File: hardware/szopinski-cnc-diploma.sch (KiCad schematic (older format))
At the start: 26 parts, among them J1 Barrel_Jack, J2 Conn_02x08_Odd_Even, J3 AVR-ISP-10, J4 Conn_01x04, J5 Conn_01x04, J6 Conn_01x04, J7 Conn_01x04, U1 ATmega328P-PU, U2 L7805, U3 DRV8825, U4 DRV8825, U5 DRV8825, U6 DRV8825, Y1 20 MHz

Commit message: Add PCB without traces
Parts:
- C1: footprint (none) -> Capacitor_THT:CP_Radial_D4.0mm_P1.50mm
- C2, C3, C4, C9: footprint (none) -> Capacitor_SMD:C_0201_0603Metric
- C5, C6, C7, C8: footprint (none) -> Capacitor_THT:CP_Radial_D6.3mm_P2.50mm
- J1: footprint (none) -> Connector_BarrelJack:BarrelJack_Horizontal
- J2: footprint (none) -> Connector_PinHeader_2.54mm:PinHeader_2x08_P2.54mm_Vertical
- J3: footprint (none) -> Connector_PinHeader_2.54mm:PinHeader_2x05_P2.54mm_Vertical
- J4, J5, J6, J7: footprint (none) -> Connector_Molex:Molex_KK-254_AE-6410-04A_1x04_P2.54mm_Vertical
- R1, R2, R3: footprint (none) -> Resistor_SMD:R_0201_0603Metric
- U2: footprint (none) -> Package_TO_SOT_THT:TO-220-3_Horizontal_TabDown
- U3, U4, U5, U6: footprint (none) -> Package_DIP:DIP-16_W15.24mm
- Y1: footprint (none) -> Crystal:Crystal_HC49-4H_Vertical
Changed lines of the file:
@@
 F 0 "U2" H 3200 1392 50  0000 C CNN
 F 1 "L7805" H 3200 1301 50  0000 C CNN
-F 2 "" H 3225 1000 50  0001 L CIN
+F 2 "Package_TO_SOT_THT:TO-220-3_Horizontal_TabDown" H 3225 1000 50  0001 L CIN
 F 3 "http://www.st.com/content/ccc/resource/technical/document/datasheet/41/4f/b3/b0/12/d4/47/88/CD00000444.pdf/files/CD00000444.pdf/jcr:content/translations/en.CD00000444.pdf" H 3200 1100 50  0001 C CNN
 	1    3200 1150
@@
 F 0 "J1" H 1407 1575 50  0000 C CNN
 F 1 "Barrel_Jack" H 1407 1484 50  0000 C CNN
-F 2 "" H 1400 1210 50  0001 C CNN
+F 2 "Connector_BarrelJack:BarrelJack_Horizontal" H 1400 1210 50  0001 C CNN
 F 3 "~" H 1400 1210 50  0001 C CNN
 	1    1350 1250
@@
 F 0 "C1" H 2618 1546 50  0000 L CNN
 F 1 "470n" H 2618 1455 50  0000 L CNN
-F 2 "" H 2538 1350 50  0001 C CNN
+F 2 "Capacitor_THT:CP_Radial_D4.0mm_P1.50mm" H 2538 1350 50  0001 C CNN
 F 3 "~" H 2500 1500 50  0001 C CNN
 	1    2500 1500
@@
 F 0 "C2" H 4315 1546 50  0000 L CNN
 F 1 "100n" H 4315 1455 50  0000 L CNN
-F 2 "" H 4238 1350 50  0001 C CNN
+F 2 "Capacitor_SMD:C_0201_0603Metric" H 4238 1350 50  0001 C CNN
 F 3 "~" H 4200 1500 50  0001 C CNN
 	1    4200 1500
@@
 F 0 "C3" H 4365 4596 50  0000 L CNN
 F 1 "22p" H 4365 4505 50  0000 L CNN
-F 2 "" H 4288 4400 50  0001 C CNN
+F 2 "Capacitor_SMD:C_0201_0603Metric" H 4288 4400 50  0001 C CNN
 F 3 "~" H 4250 4550 50  0001 C CNN
 	1    4250 4550
@@
 F 0 "Y1" H 4500 4518 50  0000 C CNN
 F 1 "20 MHz" H 4500 4427 50  0000 C CNN
-F 2 "" H 4500 4250 50  0001 C CNN
+F 2 "Crystal:Crystal_HC49-4H_Vertical" H 4500 4250 50  0001 C CNN
 F 3 "~" H 4500 4250 50  0001 C CNN
 	1    4500 4250
@@
 F 0 "R1" H 3620 4596 50  0000 L CNN
 F 1 "10k" H 3620 4505 50  0000 L CNN
-F 2 "" V 3480 4550 50  0001 C CNN
+F 2 "Resistor_SMD:R_0201_0603Metric" V 3480 4550 50  0001 C CNN
 F 3 "~" H 3550 4550 50  0001 C CNN
 	1    3550 4550
@@
 F 0 "J3" H 4470 3396 50  0000 R CNN
 F 1 "AVR-ISP-10" H 4470 3305 50  0000 R CNN
-F 2 "" V 4550 3350 50  0001 C CNN
+F 2 "Connector_PinHeader_2.54mm:PinHeader_2x05_P2.54mm_Vertical" V 4550 3350 50  0001 C CNN
 F 3 " ~" H 3525 2750 50  0001 C CNN
 	1    4800 3300
@@
 F 0 "C4" H 4865 4596 50  0000 L CNN
 F 1 "22p" H 4865 4505 50  0000 L CNN
-F 2 "" H 4788 4400 50  0001 C CNN
+F 2 "Capacitor_SMD:C_0201_0603Metric" H 4788 4400 50  0001 C CNN
 F 3 "~" H 4750 4550 50  0001 C CNN
 	1    4750 4550
@@
 F 0 "C5" V 6145 1500 50  0000 C CNN
 F 1 "CP" V 6236 1500 50  0000 C CNN
-F 2 "" H 6438 1350 50  0001 C CNN
+F 2 "Capacitor_THT:CP_Radial_D6.3mm_P2.50mm" H 6438 1350 50  0001 C CNN
 F 3 "~" H 6400 1500 50  0001 C CNN
 	1    6400 1500
@@
 F 0 "J4" V 7164 1112 50  0000 R CNN
 F 1 "Conn_01x04" V 7073 1112 50  0000 R CNN
-F 2 "" H 7200 1400 50  0001 C CNN
+F 2 "Connector_Molex:Molex_KK-254_AE-6410-04A_1x04_P2.54mm_Vertical" H 7200 1400 50  0001 C CNN
 F 3 "~" H 7200 1400 50  0001 C CNN
 	1    7200 1400
@@
 F 0 "C7" V 9045 1500 50  0000 C CNN
 F 1 "CP" V 9136 1500 50  0000 C CNN
-F 2 "" H 9338 1350 50  0001 C CNN
+F 2 "Capacitor_THT:CP_Radial_D6.3mm_P2.50mm" H 9338 1350 50  0001 C CNN
 F 3 "~" H 9300 1500 50  0001 C CNN
 	1    9300 1500
@@
 F 0 "J6" V 10064 1112 50  0000 R CNN
 F 1 "Conn_01x04" V 9973 1112 50  0000 R CNN
-F 2 "" H 10100 1400 50  0001 C CNN
+F 2 "Connector_Molex:Molex_KK-254_AE-6410-04A_1x04_P2.54mm_Vertical" H 10100 1400 50  0001 C CNN
 F 3 "~" H 10100 1400 50  0001 C CNN
 	1    10100 1400
@@
 F 0 "C6" V 6145 4100 50  0000 C CNN
 F 1 "CP" V 6236 4100 50  0000 C CNN
-F 2 "" H 6438 3950 50  0001 C CNN
+F 2 "Capacitor_THT:CP_Radial_D6.3mm_P2.50mm" H 6438 3950 50  0001 C CNN
 F 3 "~" H 6400 4100 50  0001 C CNN
 	1    6400 4100
@@
 F 0 "J5" V 7164 3712 50  0000 R CNN
 F 1 "Conn_01x04" V 7073 3712 50  0000 R CNN
-F 2 "" H 7200 4000 50  0001 C CNN
+F 2 "Connector_Molex:Molex_KK-254_AE-6410-04A_1x04_P2.54mm_Vertical" H 7200 4000 50  0001 C CNN
 F 3 "~" H 7200 4000 50  0001 C CNN
 	1    7200 4000
@@
 F 0 "C8" V 9045 4100 50  0000 C CNN
 F 1 "CP" V 9136 4100 50  0000 C CNN
-F 2 "" H 9338 3950 50  0001 C CNN
+F 2 "Capacitor_THT:CP_Radial_D6.3mm_P2.50mm" H 9338 3950 50  0001 C CNN
 F 3 "~" H 9300 4100 50  0001 C CNN
 	1    9300 4100
@@
 F 0 "J7" V 10064 3712 50  0000 R CNN
 F 1 "Conn_01x04" V 9973 3712 50  0000 R CNN
-F 2 "" H 10100 4000 50  0001 C CNN
+F 2 "Connector_Molex:Molex_KK-254_AE-6410-04A_1x04_P2.54mm_Vertical" H 10100 4000 50  0001 C CNN
 F 3 "~" H 10100 4000 50  0001 C CNN
 	1    10100 4000
@@
 F 0 "U3" H 7528 1096 50  0000 L CNN
 F 1 "DRV8825" H 7528 1005 50  0000 L CNN
-F 2 "" H 7550 1100 50  0001 C CNN
+F 2 "Package_DIP:DIP-16_W15.24mm" H 7550 1100 50  0001 C CNN
 F 3 "" H 7550 1100 50  0001 C CNN
 	1    6850 1700
@@
 F 0 "U5" H 10428 1096 50  0000 L CNN
 F 1 "DRV8825" H 10428 1005 50  0000 L CNN
-F 2 "" H 10450 1100 50  0001 C CNN
+F 2 "Package_DIP:DIP-16_W15.24mm" H 10450 1100 50  0001 C CNN
 F 3 "" H 10450 1100 50  0001 C CNN
 	1    9750 1700
@@
 F 0 "U6" H 10428 3696 50  0000 L CNN
 F 1 "DRV8825" H 10428 3605 50  0000 L CNN
-F 2 "" H 10450 3700 50  0001 C CNN
+F 2 "Package_DIP:DIP-16_W15.24mm" H 10450 3700 50  0001 C CNN
 F 3 "" H 10450 3700 50  0001 C CNN
 	1    9750 4300
@@
 F 0 "U4" H 7528 3696 50  0000 L CNN
 F 1 "DRV8825" H 7528 3605 50  0000 L CNN
-F 2 "" H 7550 3700 50  0001 C CNN
+F 2 "Package_DIP:DIP-16_W15.24mm" H 7550 3700 50  0001 C CNN
 F 3 "" H 7550 3700 50  0001 C CNN
 	1    6850 4300
@@
 F 0 "R2" H 5520 5196 50  0000 L CNN
 F 1 "10k" H 5520 5105 50  0000 L CNN
-F 2 "" V 5380 5150 50  0001 C CNN
+F 2 "Resistor_SMD:R_0201_0603Metric" V 5380 5150 50  0001 C CNN
 F 3 "~" H 5450 5150 50  0001 C CNN
 	1    5450 5150
@@
 F 0 "R3" H 5570 2146 50  0000 L CNN
 F 1 "10k" H 5570 2055 50  0000 L CNN
-F 2 "" V 5430 2100 50  0001 C CNN
+F 2 "Resistor_SMD:R_0201_0603Metric" V 5430 2100 50  0001 C CNN
 F 3 "~" H 5500 2100 50  0001 C CNN
 	1    5500 2100
@@
 F 0 "J2" H 4500 6917 50  0000 C CNN
 F 1 "Conn_02x08_Odd_Even" H 4500 6826 50  0000 C CNN
-F 2 "" H 4450 6400 50  0001 C CNN
+F 2 "Connector_PinHeader_2.54mm:PinHeader_2x08_P2.54mm_Vertical" H 4450 6400 50  0001 C CNN
 F 3 "~" H 4450 6400 50  0001 C CNN
 	1    4450 6400
@@
 F 0 "C9" V 1748 2600 50  0000 C CNN
 F 1 "100n" V 1839 2600 50  0000 C CNN
-F 2 "" H 2038 2450 50  0001 C CNN
+F 2 "Capacitor_SMD:C_0201_0603Metric" H 2038 2450 50  0001 C CNN
 F 3 "~" H 2000 2600 50  0001 C CNN
 	1    2000 2600

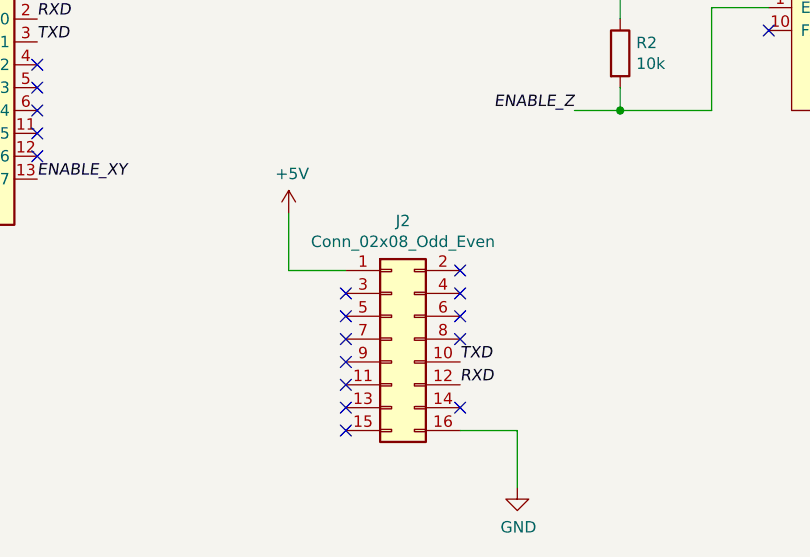
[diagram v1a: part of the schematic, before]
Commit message: Fix footprints, symbols and clearance issues
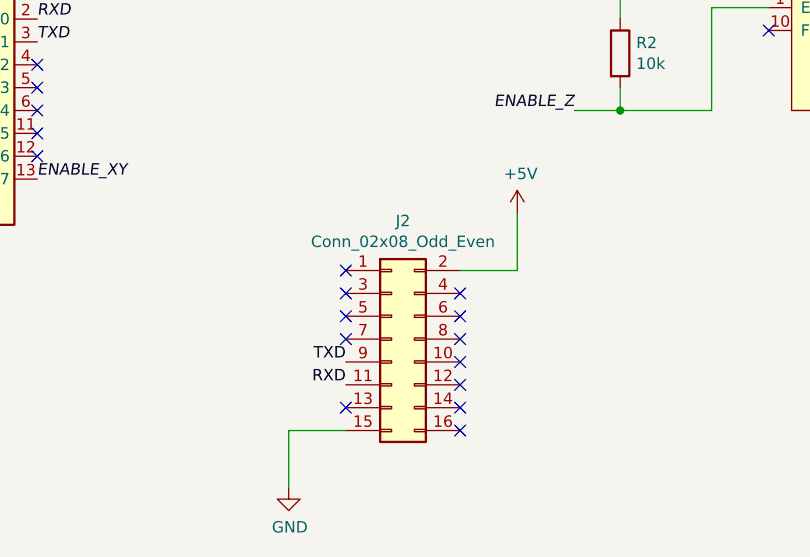
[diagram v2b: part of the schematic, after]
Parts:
- C2, C9: footprint Capacitor_SMD:C_0201_0603Metric -> Capacitor_SMD:C_1206_3216Metric
- C3, C4: footprint Capacitor_SMD:C_0201_0603Metric -> Capacitor_SMD:C_0805_2012Metric
- J2: footprint Connector_PinHeader_2.54mm:PinHeader_2x08_P2.54mm_Vertical -> Connector_PinSocket_2.54mm:PinSocket_2x08_P2.54mm_Vertical
- R1, R2, R3: footprint Resistor_SMD:R_0201_0603Metric -> Resistor_SMD:R_1206_3216Metric
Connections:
- net +5V: now also J2.2 (Pin_2); no longer J2.1 (Pin_1)
- net GND: now also J2.15 (Pin_15); no longer J2.16 (Pin_16)
- net RXD: now also J2.11 (Pin_11); no longer J2.12 (Pin_12)
- net TXD: now also J2.9 (Pin_9); no longer J2.10 (Pin_10)
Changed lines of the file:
@@
 F 0 "C2" H 4315 1546 50  0000 L CNN
 F 1 "100n" H 4315 1455 50  0000 L CNN
-F 2 "Capacitor_SMD:C_0201_0603Metric" H 4238 1350 50  0001 C CNN
+F 2 "Capacitor_SMD:C_1206_3216Metric" H 4238 1350 50  0001 C CNN
 F 3 "~" H 4200 1500 50  0001 C CNN
 	1    4200 1500
@@
 F 0 "C3" H 4365 4596 50  0000 L CNN
 F 1 "22p" H 4365 4505 50  0000 L CNN
-F 2 "Capacitor_SMD:C_0201_0603Metric" H 4288 4400 50  0001 C CNN
+F 2 "Capacitor_SMD:C_0805_2012Metric" H 4288 4400 50  0001 C CNN
 F 3 "~" H 4250 4550 50  0001 C CNN
 	1    4250 4550
@@
 F 0 "R1" H 3620 4596 50  0000 L CNN
 F 1 "10k" H 3620 4505 50  0000 L CNN
-F 2 "Resistor_SMD:R_0201_0603Metric" V 3480 4550 50  0001 C CNN
+F 2 "Resistor_SMD:R_1206_3216Metric" V 3480 4550 50  0001 C CNN
 F 3 "~" H 3550 4550 50  0001 C CNN
 	1    3550 4550
@@
 F 0 "C4" H 4865 4596 50  0000 L CNN
 F 1 "22p" H 4865 4505 50  0000 L CNN
-F 2 "Capacitor_SMD:C_0201_0603Metric" H 4788 4400 50  0001 C CNN
+F 2 "Capacitor_SMD:C_0805_2012Metric" H 4788 4400 50  0001 C CNN
 F 3 "~" H 4750 4550 50  0001 C CNN
 	1    4750 4550
@@
 F 0 "R2" H 5520 5196 50  0000 L CNN
 F 1 "10k" H 5520 5105 50  0000 L CNN
-F 2 "Resistor_SMD:R_0201_0603Metric" V 5380 5150 50  0001 C CNN
+F 2 "Resistor_SMD:R_1206_3216Metric" V 5380 5150 50  0001 C CNN
 F 3 "~" H 5450 5150 50  0001 C CNN
 	1    5450 5150
@@
 F 0 "R3" H 5570 2146 50  0000 L CNN
 F 1 "10k" H 5570 2055 50  0000 L CNN
-F 2 "Resistor_SMD:R_0201_0603Metric" V 5430 2100 50  0001 C CNN
+F 2 "Resistor_SMD:R_1206_3216Metric" V 5430 2100 50  0001 C CNN
 F 3 "~" H 5500 2100 50  0001 C CNN
 	1    5500 2100
@@
 F 0 "J2" H 4500 6917 50  0000 C CNN
 F 1 "Conn_02x08_Odd_Even" H 4500 6826 50  0000 C CNN
-F 2 "Connector_PinHeader_2.54mm:PinHeader_2x08_P2.54mm_Vertical" H 4450 6400 50  0001 C CNN
+F 2 "Connector_PinSocket_2.54mm:PinSocket_2x08_P2.54mm_Vertical" H 4450 6400 50  0001 C CNN
 F 3 "~" H 4450 6400 50  0001 C CNN
 	1    4450 6400
@@
 L power:+5V #PWR0128
 U 1 1 631A455B
-P 4000 5850
-F 0 "#PWR0128" H 4000 5700 50  0001 C CNN
-F 1 "+5V" H 4015 6023 50  0000 C CNN
-F 2 "" H 4000 5850 50  0001 C CNN
-F 3 "" H 4000 5850 50  0001 C CNN
-	1    4000 5850
-	1    0    0    -1
-$EndComp
-Wire Wire Line
-	4000 5850 4000 6100
-Wire Wire Line
-	4000 6100 4250 6100
+P 5000 5850
+F 0 "#PWR0128" H 5000 5700 50  0001 C CNN
+F 1 "+5V" H 5015 6023 50  0000 C CNN
+F 2 "" H 5000 5850 50  0001 C CNN
+F 3 "" H 5000 5850 50  0001 C CNN
+	1    5000 5850
+	1    0    0    -1
+$EndComp
+Wire Wire Line
+	5000 5850 5000 6100
+Wire Wire Line
+	4750 6100 5000 6100
 $Comp
 L power:GND #PWR0129
 U 1 1 631AB985
-P 5000 7050
-F 0 "#PWR0129" H 5000 6800 50  0001 C CNN
-F 1 "GND" H 5005 6877 50  0000 C CNN
-F 2 "" H 5000 7050 50  0001 C CNN
-F 3 "" H 5000 7050 50  0001 C CNN
-	1    5000 7050
-	1    0    0    -1
-$EndComp
-Wire Wire Line
-	4750 6800 5000 6800
-Wire Wire Line
-	5000 6800 5000 7050
-NoConn ~ 4750 6100
+P 4000 7050
+F 0 "#PWR0129" H 4000 6800 50  0001 C CNN
+F 1 "GND" H 4005 6877 50  0000 C CNN
+F 2 "" H 4000 7050 50  0001 C CNN
+F 3 "" H 4000 7050 50  0001 C CNN
+	1    4000 7050
+	1    0    0    -1
+$EndComp
+Wire Wire Line
+	4000 6800 4250 6800
+Wire Wire Line
+	4000 6800 4000 7050
 NoConn ~ 4750 6200
 NoConn ~ 4750 6300
@@
 NoConn ~ 4250 6300
 NoConn ~ 4250 6400
-NoConn ~ 4250 6500
-NoConn ~ 4250 6600
 NoConn ~ 4250 6700
-NoConn ~ 4250 6800
 NoConn ~ 2900 5200
 NoConn ~ 2900 5300
@@
 Text Label 2900 5000 0    50   Italic 0
 RXD
-Text Label 4750 6600 0    50   Italic 0
-RXD
 Text Label 2900 5100 0    50   Italic 0
-TXD
-Text Label 4750 6500 0    50   Italic 0
 TXD
 $Comp
@@
 F 0 "C9" V 1748 2600 50  0000 C CNN
 F 1 "100n" V 1839 2600 50  0000 C CNN
-F 2 "Capacitor_SMD:C_0201_0603Metric" H 2038 2450 50  0001 C CNN
+F 2 "Capacitor_SMD:C_1206_3216Metric" H 2038 2450 50  0001 C CNN
 F 3 "~" H 2000 2600 50  0001 C CNN
 	1    2000 2600
@@
 Wire Wire Line
 	2300 2300 2300 2600
+NoConn ~ 4250 6100
+Text Label 4250 6500 2    50   ~ 0
+TXD
+Text Label 4250 6600 2    50   ~ 0
+RXD
+NoConn ~ 4750 6500
+NoConn ~ 4750 6600
+NoConn ~ 4750 6800
 $EndSCHEMATC

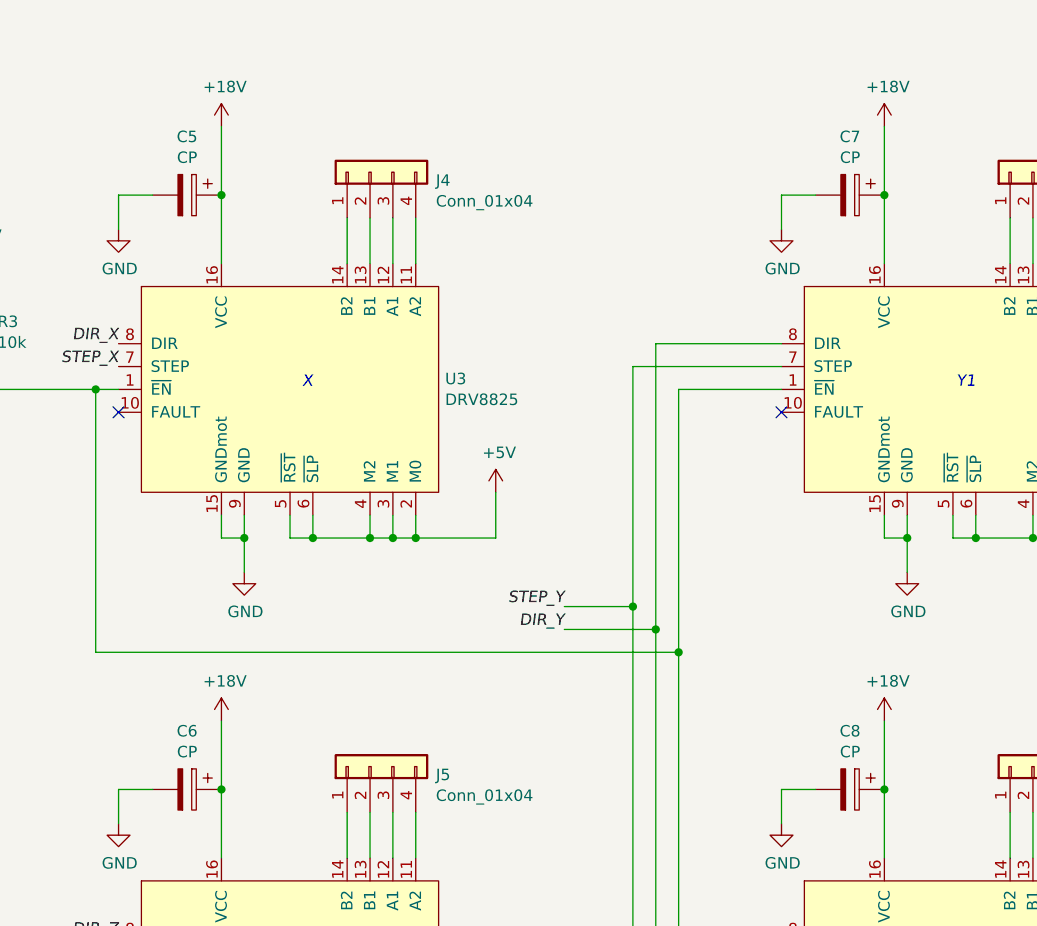
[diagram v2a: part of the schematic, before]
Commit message: Add value for driver capacitors
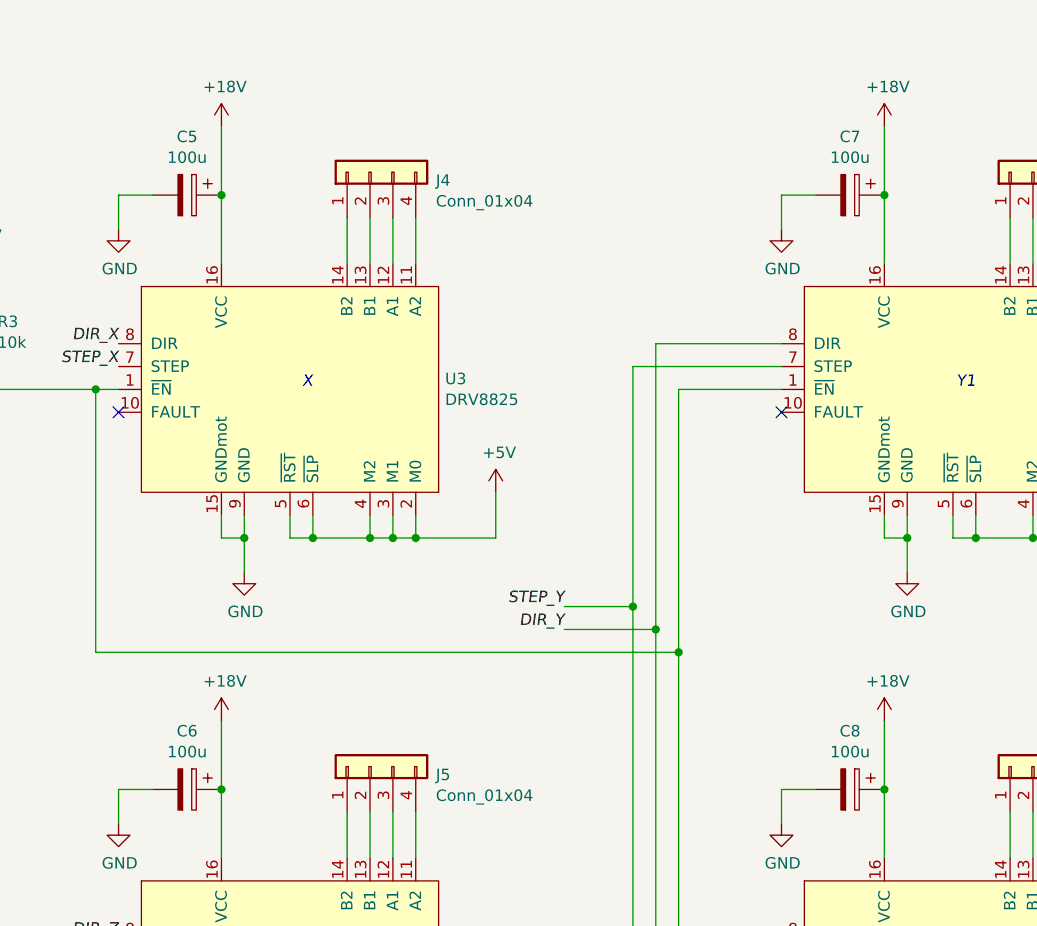
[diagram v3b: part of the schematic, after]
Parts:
- C5, C6, C7, C8: value CP -> 100u
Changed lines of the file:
@@
 P 6400 1500
 F 0 "C5" V 6145 1500 50  0000 C CNN
-F 1 "CP" V 6236 1500 50  0000 C CNN
+F 1 "100u" V 6236 1500 50  0000 C CNN
 F 2 "Capacitor_THT:CP_Radial_D6.3mm_P2.50mm" H 6438 1350 50  0001 C CNN
 F 3 "~" H 6400 1500 50  0001 C CNN
@@
 P 9300 1500
 F 0 "C7" V 9045 1500 50  0000 C CNN
-F 1 "CP" V 9136 1500 50  0000 C CNN
+F 1 "100u" V 9136 1500 50  0000 C CNN
 F 2 "Capacitor_THT:CP_Radial_D6.3mm_P2.50mm" H 9338 1350 50  0001 C CNN
 F 3 "~" H 9300 1500 50  0001 C CNN
@@
 P 6400 4100
 F 0 "C6" V 6145 4100 50  0000 C CNN
-F 1 "CP" V 6236 4100 50  0000 C CNN
+F 1 "100u" V 6236 4100 50  0000 C CNN
 F 2 "Capacitor_THT:CP_Radial_D6.3mm_P2.50mm" H 6438 3950 50  0001 C CNN
 F 3 "~" H 6400 4100 50  0001 C CNN
@@
 P 9300 4100
 F 0 "C8" V 9045 4100 50  0000 C CNN
-F 1 "CP" V 9136 4100 50  0000 C CNN
+F 1 "100u" V 9136 4100 50  0000 C CNN
 F 2 "Capacitor_THT:CP_Radial_D6.3mm_P2.50mm" H 9338 3950 50  0001 C CNN
 F 3 "~" H 9300 4100 50  0001 C CNN

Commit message: Redesign PCB
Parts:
- C2, C9: footprint Capacitor_SMD:C_1206_3216Metric -> Capacitor_THT:C_Disc_D6.0mm_W4.4mm_P5.00mm
- C3, C4: footprint Capacitor_SMD:C_0805_2012Metric -> Capacitor_THT:C_Disc_D6.0mm_W4.4mm_P5.00mm
- R1, R2, R3: footprint Resistor_SMD:R_1206_3216Metric -> Resistor_THT:R_Axial_DIN0207_L6.3mm_D2.5mm_P7.62mm_Horizontal
- U2: footprint Package_TO_SOT_THT:TO-220-3_Horizontal_TabDown -> Package_TO_SOT_THT:TO-220-3_Vertical
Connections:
- net ENABLE_XY: now also U1.4 (PD2); no longer U1.13 (PD7)
- net ENABLE_Z: now also U1.15 (PB1); no longer U1.14 (PB0)
- no-connect marks 25 -> 26
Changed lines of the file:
@@
 F 0 "U2" H 3200 1392 50  0000 C CNN
 F 1 "L7805" H 3200 1301 50  0000 C CNN
-F 2 "Package_TO_SOT_THT:TO-220-3_Horizontal_TabDown" H 3225 1000 50  0001 L CIN
+F 2 "Package_TO_SOT_THT:TO-220-3_Vertical" H 3225 1000 50  0001 L CIN
 F 3 "http://www.st.com/content/ccc/resource/technical/document/datasheet/41/4f/b3/b0/12/d4/47/88/CD00000444.pdf/files/CD00000444.pdf/jcr:content/translations/en.CD00000444.pdf" H 3200 1100 50  0001 C CNN
 	1    3200 1150
@@
 F 0 "C2" H 4315 1546 50  0000 L CNN
 F 1 "100n" H 4315 1455 50  0000 L CNN
-F 2 "Capacitor_SMD:C_1206_3216Metric" H 4238 1350 50  0001 C CNN
+F 2 "Capacitor_THT:C_Disc_D6.0mm_W4.4mm_P5.00mm" H 4238 1350 50  0001 C CNN
 F 3 "~" H 4200 1500 50  0001 C CNN
 	1    4200 1500
@@
 F 0 "C3" H 4365 4596 50  0000 L CNN
 F 1 "22p" H 4365 4505 50  0000 L CNN
-F 2 "Capacitor_SMD:C_0805_2012Metric" H 4288 4400 50  0001 C CNN
+F 2 "Capacitor_THT:C_Disc_D6.0mm_W4.4mm_P5.00mm" H 4288 4400 50  0001 C CNN
 F 3 "~" H 4250 4550 50  0001 C CNN
 	1    4250 4550
@@
 F 0 "R1" H 3620 4596 50  0000 L CNN
 F 1 "10k" H 3620 4505 50  0000 L CNN
-F 2 "Resistor_SMD:R_1206_3216Metric" V 3480 4550 50  0001 C CNN
+F 2 "Resistor_THT:R_Axial_DIN0207_L6.3mm_D2.5mm_P7.62mm_Horizontal" V 3480 4550 50  0001 C CNN
 F 3 "~" H 3550 4550 50  0001 C CNN
 	1    3550 4550
@@
 F 0 "C4" H 4865 4596 50  0000 L CNN
 F 1 "22p" H 4865 4505 50  0000 L CNN
-F 2 "Capacitor_SMD:C_0805_2012Metric" H 4788 4400 50  0001 C CNN
+F 2 "Capacitor_THT:C_Disc_D6.0mm_W4.4mm_P5.00mm" H 4788 4400 50  0001 C CNN
 F 3 "~" H 4750 4550 50  0001 C CNN
 	1    4750 4550
@@
 F 0 "R2" H 5520 5196 50  0000 L CNN
 F 1 "10k" H 5520 5105 50  0000 L CNN
-F 2 "Resistor_SMD:R_1206_3216Metric" V 5380 5150 50  0001 C CNN
+F 2 "Resistor_THT:R_Axial_DIN0207_L6.3mm_D2.5mm_P7.62mm_Horizontal" V 5380 5150 50  0001 C CNN
 F 3 "~" H 5450 5150 50  0001 C CNN
 	1    5450 5150
@@
 F 0 "R3" H 5570 2146 50  0000 L CNN
 F 1 "10k" H 5570 2055 50  0000 L CNN
-F 2 "Resistor_SMD:R_1206_3216Metric" V 5430 2100 50  0001 C CNN
+F 2 "Resistor_THT:R_Axial_DIN0207_L6.3mm_D2.5mm_P7.62mm_Horizontal" V 5430 2100 50  0001 C CNN
 F 3 "~" H 5500 2100 50  0001 C CNN
 	1    5500 2100
@@
 NoConn ~ 4250 6400
 NoConn ~ 4250 6700
-NoConn ~ 2900 5200
+NoConn ~ 2900 5700
 NoConn ~ 2900 5300
 NoConn ~ 2900 5400
@@
 	3500 1150 4200 1150
 NoConn ~ 2900 3500
-NoConn ~ 2900 3400
 NoConn ~ 4750 6700
 $Comp
@@
 $EndComp
 NoConn ~ 2900 5600
-Text Label 2900 3300 0    50   Italic 0
+Text Label 2900 3400 0    50   Italic 0
 ENABLE_Z
-Text Label 2900 5700 0    50   Italic 0
+Text Label 2900 5200 0    50   Italic 0
 ENABLE_XY
 Wire Wire Line
@@
 F 0 "C9" V 1748 2600 50  0000 C CNN
 F 1 "100n" V 1839 2600 50  0000 C CNN
-F 2 "Capacitor_SMD:C_1206_3216Metric" H 2038 2450 50  0001 C CNN
+F 2 "Capacitor_THT:C_Disc_D6.0mm_W4.4mm_P5.00mm" H 2038 2450 50  0001 C CNN
 F 3 "~" H 2000 2600 50  0001 C CNN
 	1    2000 2600
@@
 NoConn ~ 4750 6600
 NoConn ~ 4750 6800
+NoConn ~ 2900 3300
+NoConn ~ 4900 4000
 $EndSCHEMATC
